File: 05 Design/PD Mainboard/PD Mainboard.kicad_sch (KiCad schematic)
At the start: 0 parts

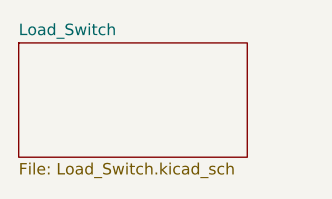
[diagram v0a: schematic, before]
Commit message: load switch with iso spi idea
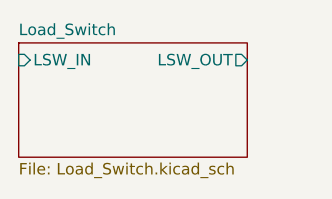
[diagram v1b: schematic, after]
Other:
- sheet Load_Switch ports: added LSW_IN, LSW_OUT; removed none
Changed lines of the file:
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@@
       (effects (font (size 1.27 1.27)) (justify left top))
     )
+    (pin "LSW_OUT" output (at 114.3 40.005 0)
+      (effects (font (size 1.27 1.27)) (justify right))
+    )
+    (pin "LSW_IN" input (at 88.9 40.005 180)
+      (effects (font (size 1.27 1.27)) (justify left))
+    )
     (instances
-      (project "74_series_UPD"
+      (project "PD Mainboard"
         (path "/9702ea92-4279-4d05-9e00-16f440ea80dd" (page "2"))
       )
